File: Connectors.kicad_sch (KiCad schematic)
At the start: 4 parts, among them J1 Conn_01x07_Pin, J2 21033213501, J4 21033213501

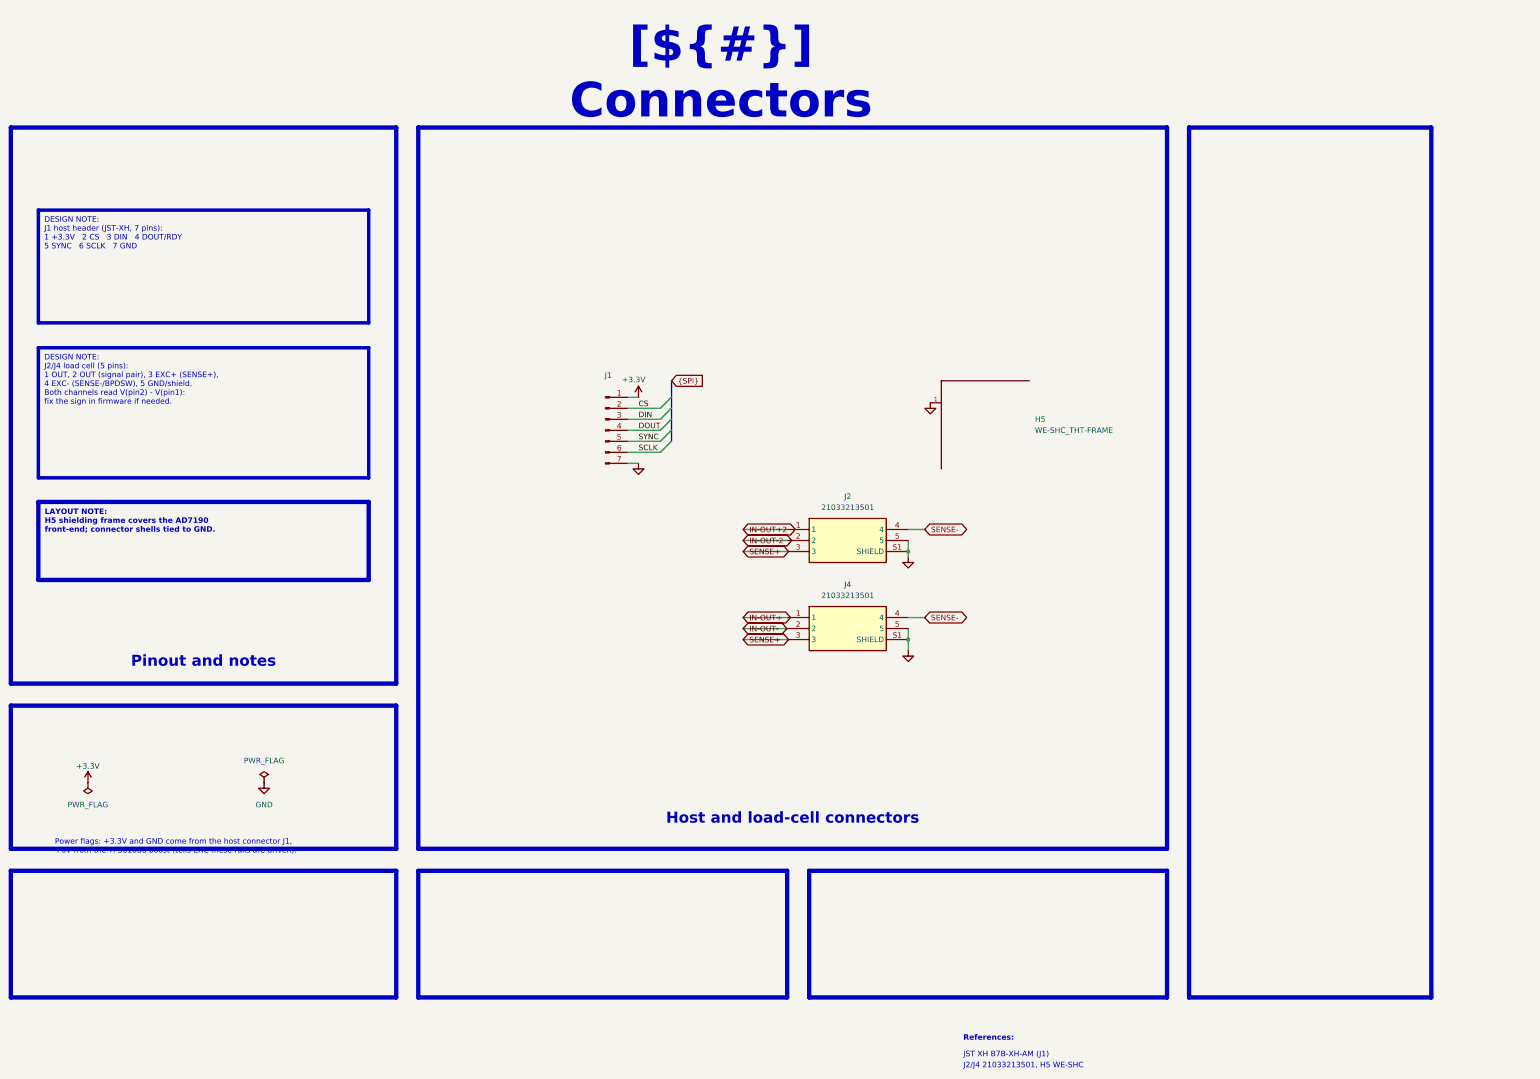
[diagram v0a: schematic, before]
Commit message: Restyle the schematic like OPEN_PHASE, merge the power sheets, rework the bottom silkscreen
- Schematic: all sheets on A3 in the OPEN_PHASE look (red header bands,
  DESCRIPTION / DESIGN NOTE / LAYOUT NOTE / CALCULS & BUDGET panels in
  French, TEST POINTS panel, References in the title block)
- Title block: INGENIERIE FRANCE logo in KDT_Template_GIT.kicad_wks,
  per-sheet logo images removed
- Power - Sequencing rebuilt with curves from LTspice simulations 01-04
- TPS61086 and LT3042 sheets merged into Power Supply - Analog Rails
  (page 5, keeps the TPS sheet UUID); pages renumbered to 9, local nets
  renamed to /Project Architecture/Power_Supply/*, PCB links updated
- PCB: per-rail net colours (+3.3V, +6V, +5VA, GND) as on OPEN_PHASE
- PCB B.SilkS: test point pills with Arial Black knockout names, J1
  pinout cells, E+/E-/S+/S- tags on the M12 pads, CELL 1 / CELL 2 titles
  and a LOAD CELL wiring panel

Netlist connectivity, ERC (2 warnings) and copper DRC unchanged;
schematic parity clean.

Co-Authored-By: Claude Opus 5.5 <noreply@anthropic.com>
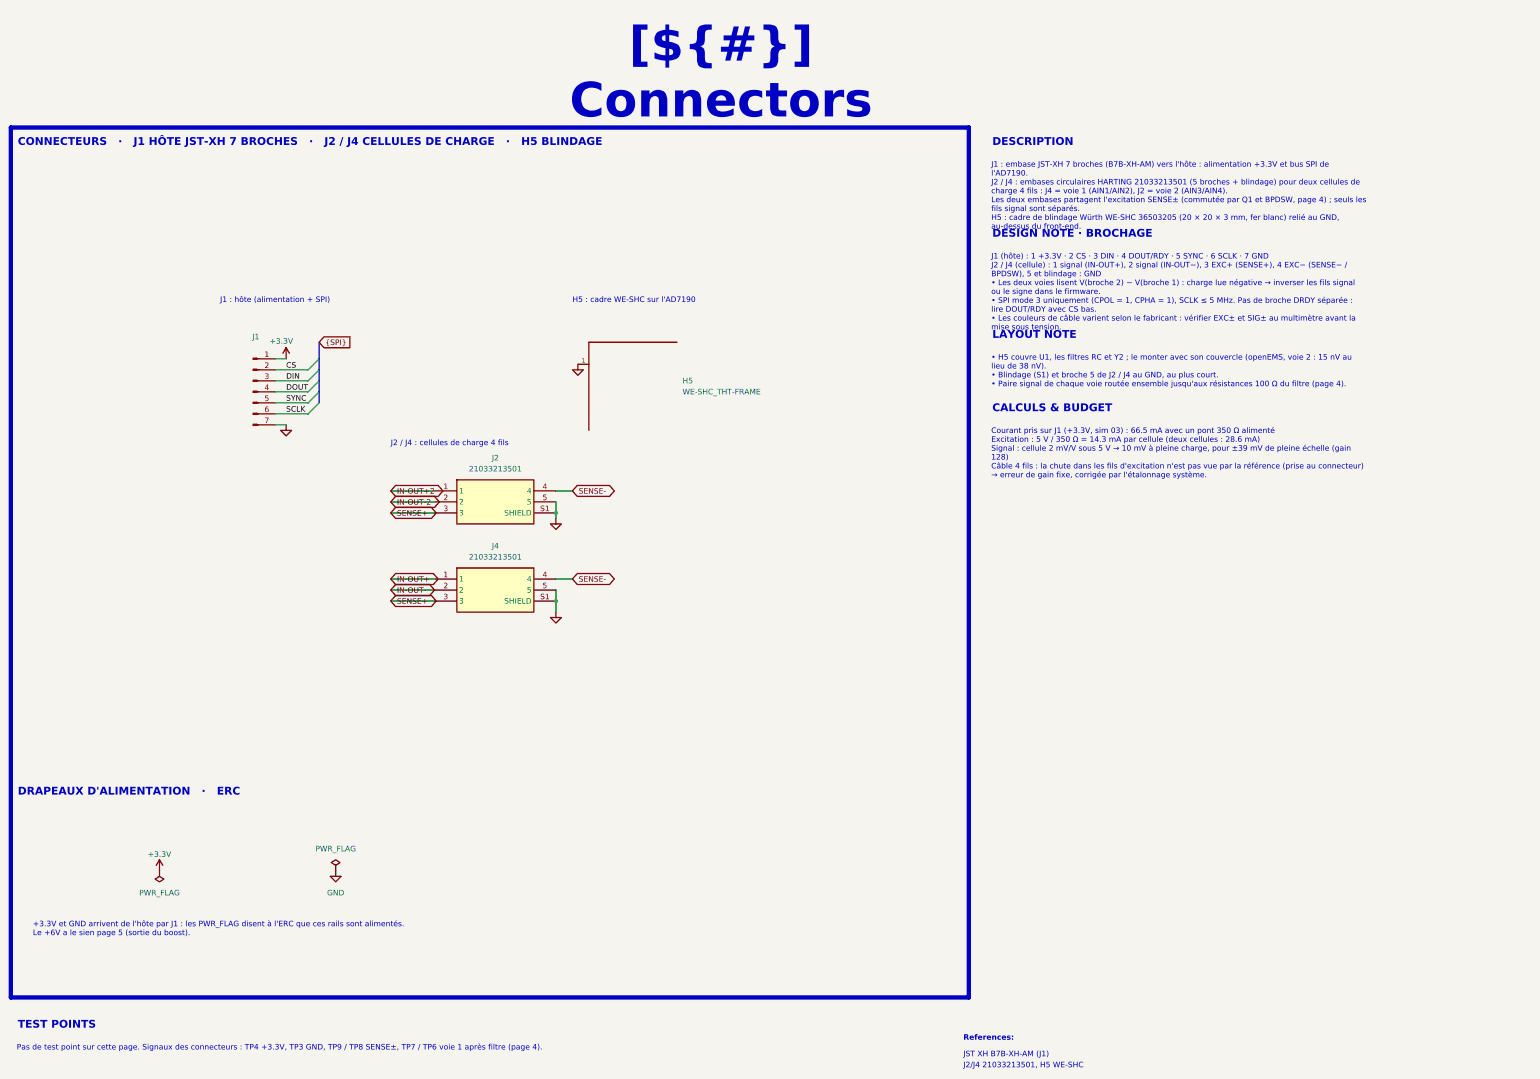
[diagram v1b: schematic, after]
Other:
- note added: "+3.3V et GND arrivent de l'hôte par J1 : les PWR_FLAG disent à l'ERC que ces rails sont alimentés. Le +6V a le sien page 5 (sortie du boost)."
- note added: "H5 : cadre WE-SHC sur l'AD7190"
- note added: "J1 : hôte (alimentation + SPI)"
- note added: "J2 / J4 : cellules de charge 4 fils"
- note removed: "Power flags: +3.3V and GND come from the host connector J1, +6V from the TPS61086 boost (tells ERC these rails are driven)."
- moved on the sheet: H5, J1, J2, J4
